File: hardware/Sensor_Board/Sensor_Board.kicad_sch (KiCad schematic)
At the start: 0 parts

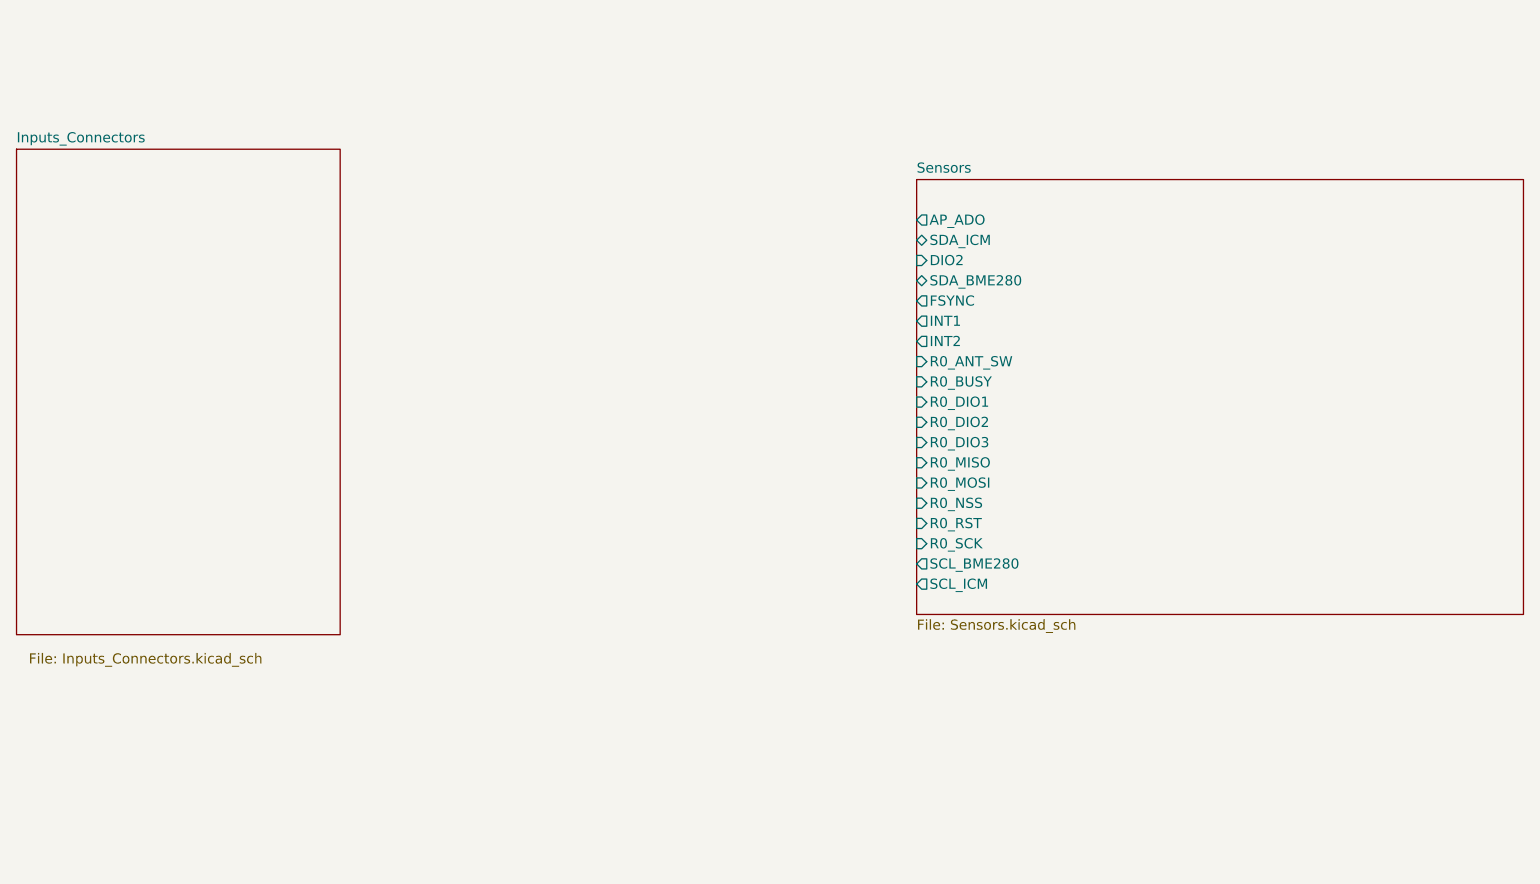
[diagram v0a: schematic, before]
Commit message: feat(Hw):Batt_Board_Pro_Added
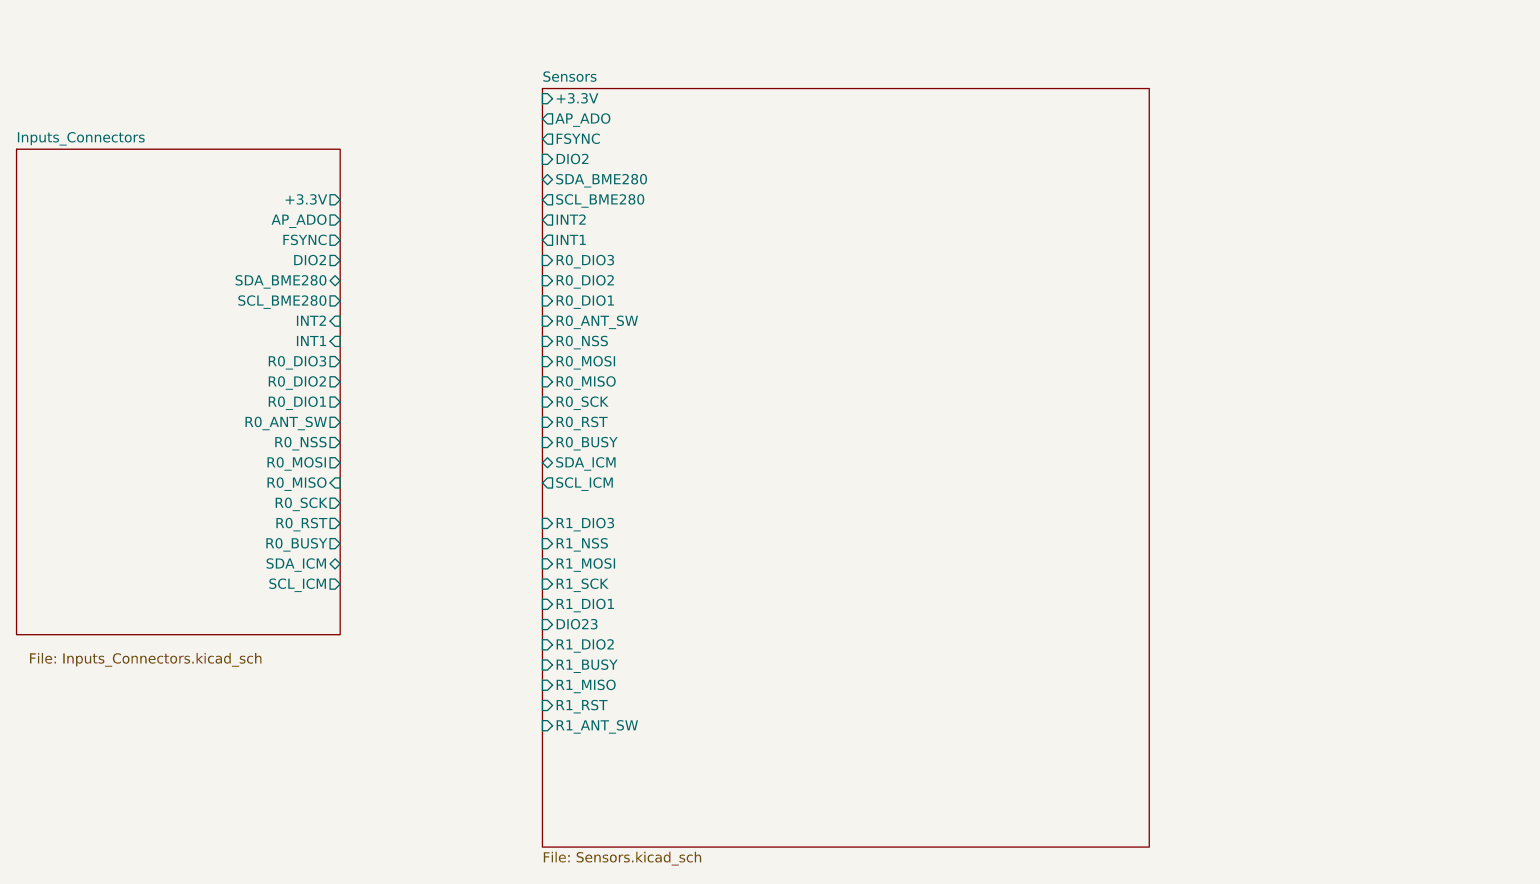
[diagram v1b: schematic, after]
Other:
- sheet Inputs_Connectors ports: added +3.3V, AP_ADO, DIO2, FSYNC, INT1, INT2, R0_ANT_SW, R0_BUSY, R0_DIO1, R0_DIO2, R0_DIO3, R0_MISO, R0_MOSI, R0_NSS, R0_RST, R0_SCK, SCL_BME280, SCL_ICM, SDA_BME280, SDA_ICM; removed none
- sheet Sensors ports: added +3.3V, DIO23, R1_ANT_SW, R1_BUSY, R1_DIO1, R1_DIO2, R1_DIO3, R1_MISO, R1_MOSI, R1_NSS, R1_RST, R1_SCK; removed none

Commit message: feat(Hw):floorplans_updated
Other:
- sheet Inputs_Connectors ports: added DIO23, R1_ANT_SW, R1_BUSY, R1_DIO1, R1_DIO2, R1_DIO3, R1_MISO, R1_MOSI, R1_NSS, R1_RST, R1_SCK; removed none

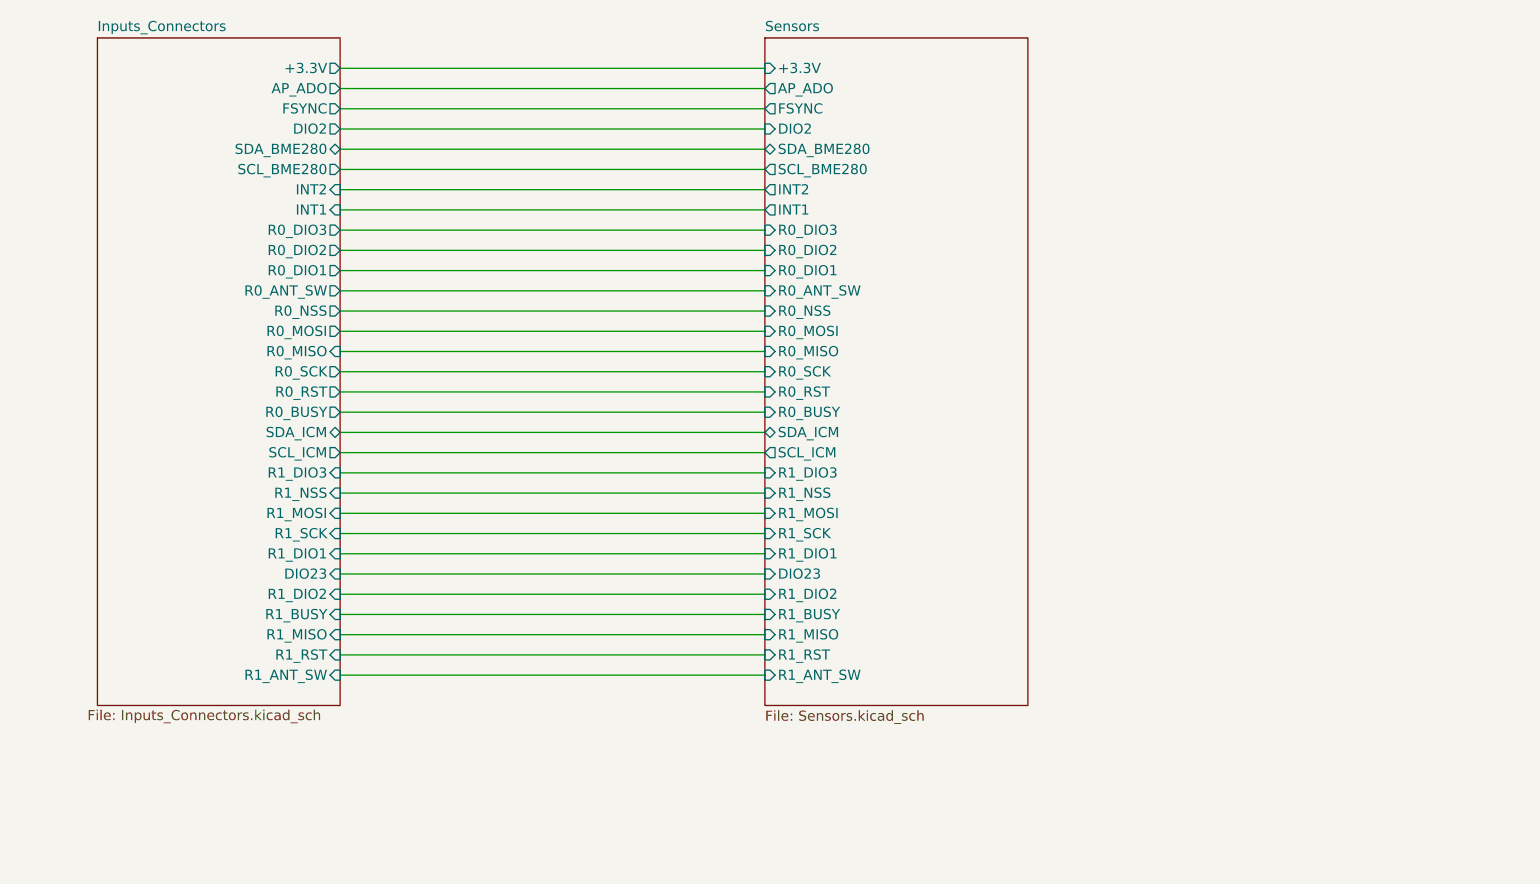
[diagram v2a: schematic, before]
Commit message: fix(Hw):Tracks_modified
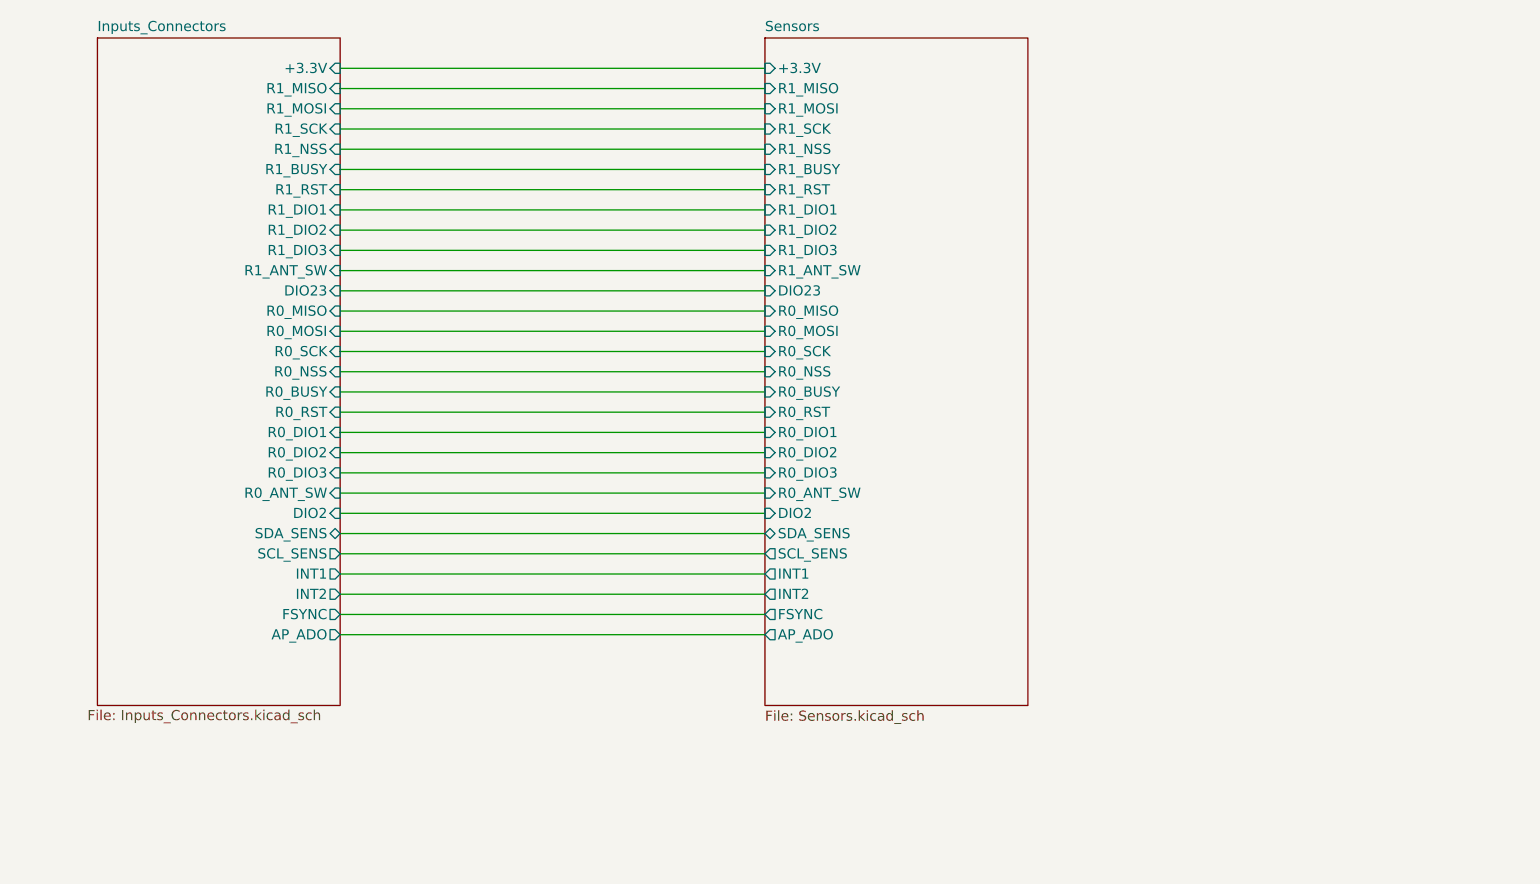
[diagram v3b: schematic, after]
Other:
- sheet Inputs_Connectors ports: added SCL_SENS, SDA_SENS; removed SCL_BME280, SCL_ICM, SDA_BME280, SDA_ICM
- sheet Sensors ports: added SCL_SENS, SDA_SENS; removed SCL_BME280, SCL_ICM, SDA_BME280, SDA_ICM

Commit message: feat(Hw):BME280_Moved
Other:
- company: (none) -> Electronic Cats
- title: (none) -> Sensor_Board
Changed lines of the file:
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@@
 	(generator_version "9.0")
 	(paper "A4")
+	(title_block
+		(title "Sensor_Board")
+		(date "2026-02-06")
+		(rev "1.0")
+		(company "Electronic Cats")
+		(comment 1 "Edgar Capuchino")
+	)
 	(wire
 		(pts
